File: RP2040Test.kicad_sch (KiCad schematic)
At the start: 1 part

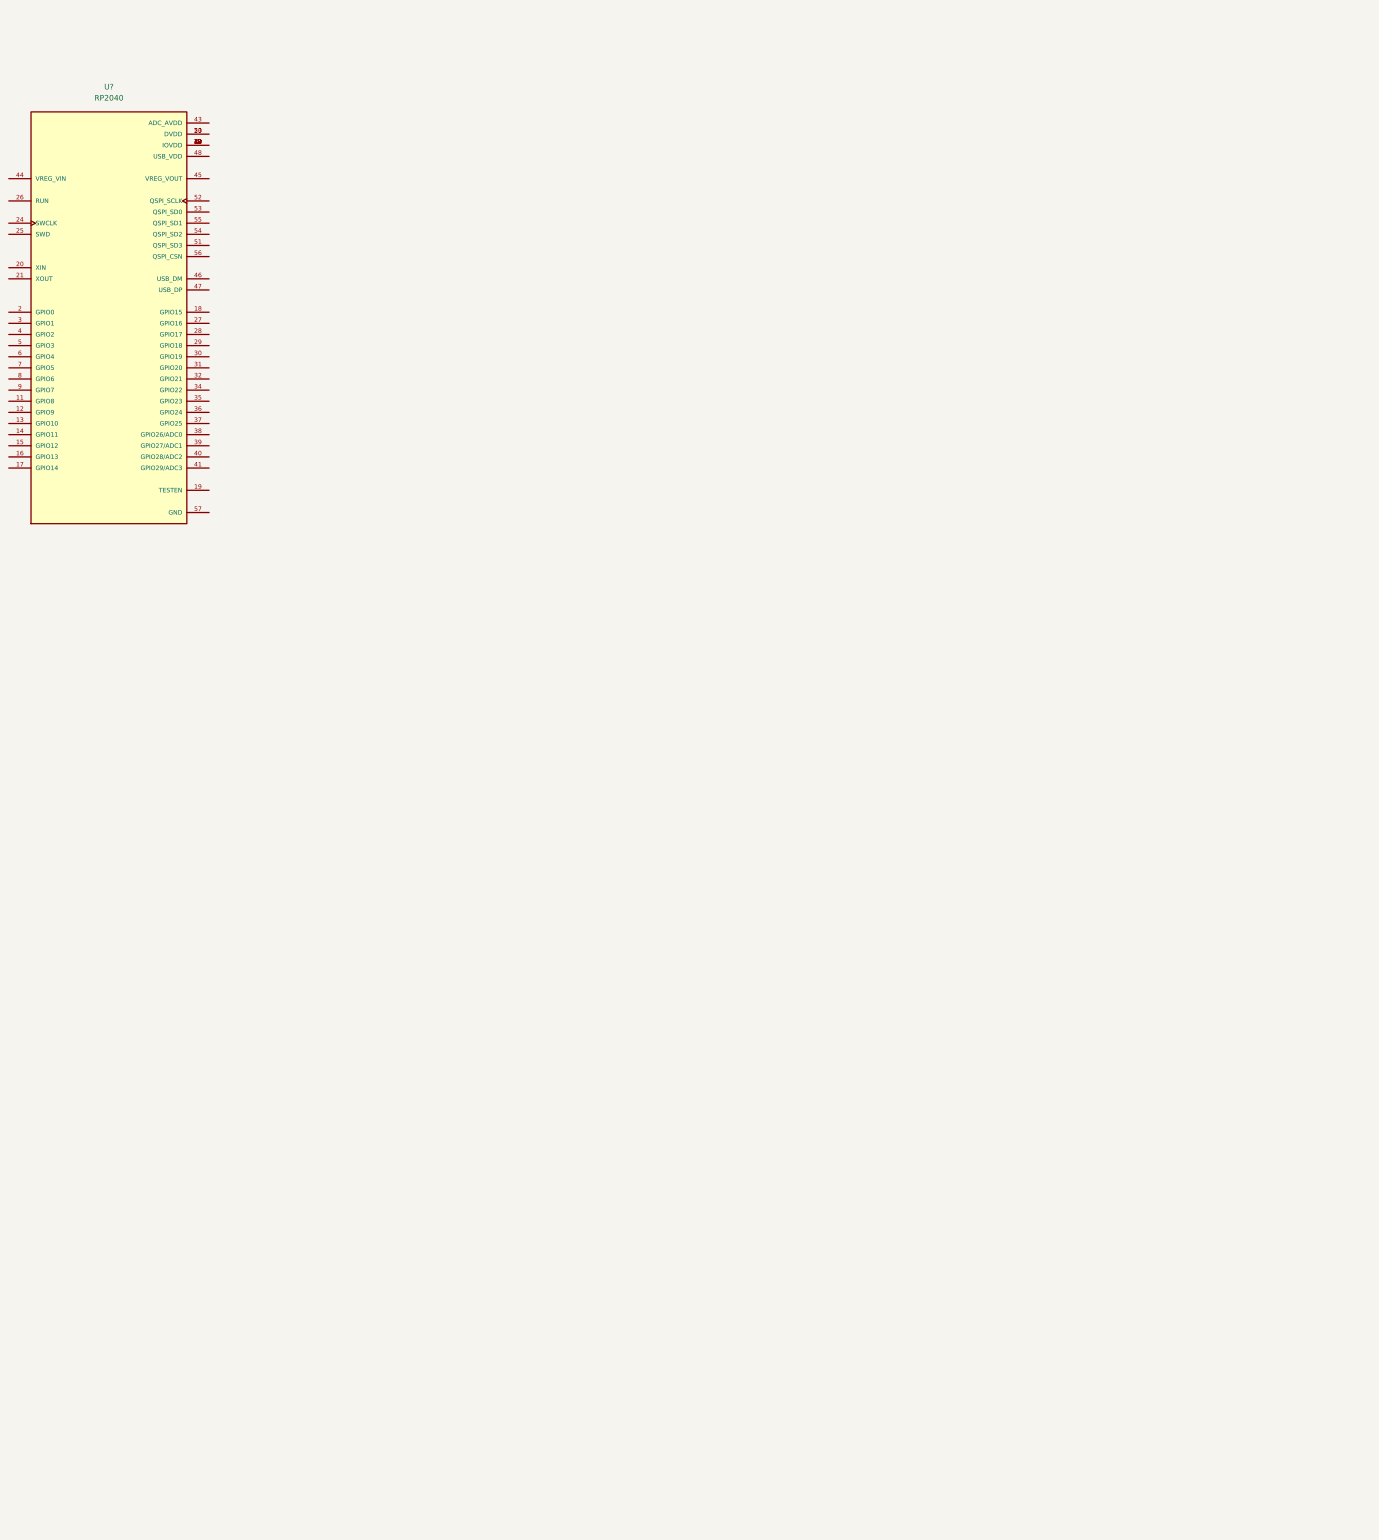
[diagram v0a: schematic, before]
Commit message: laid out electronics for mcu usb and solenoid, double check how power supply will work
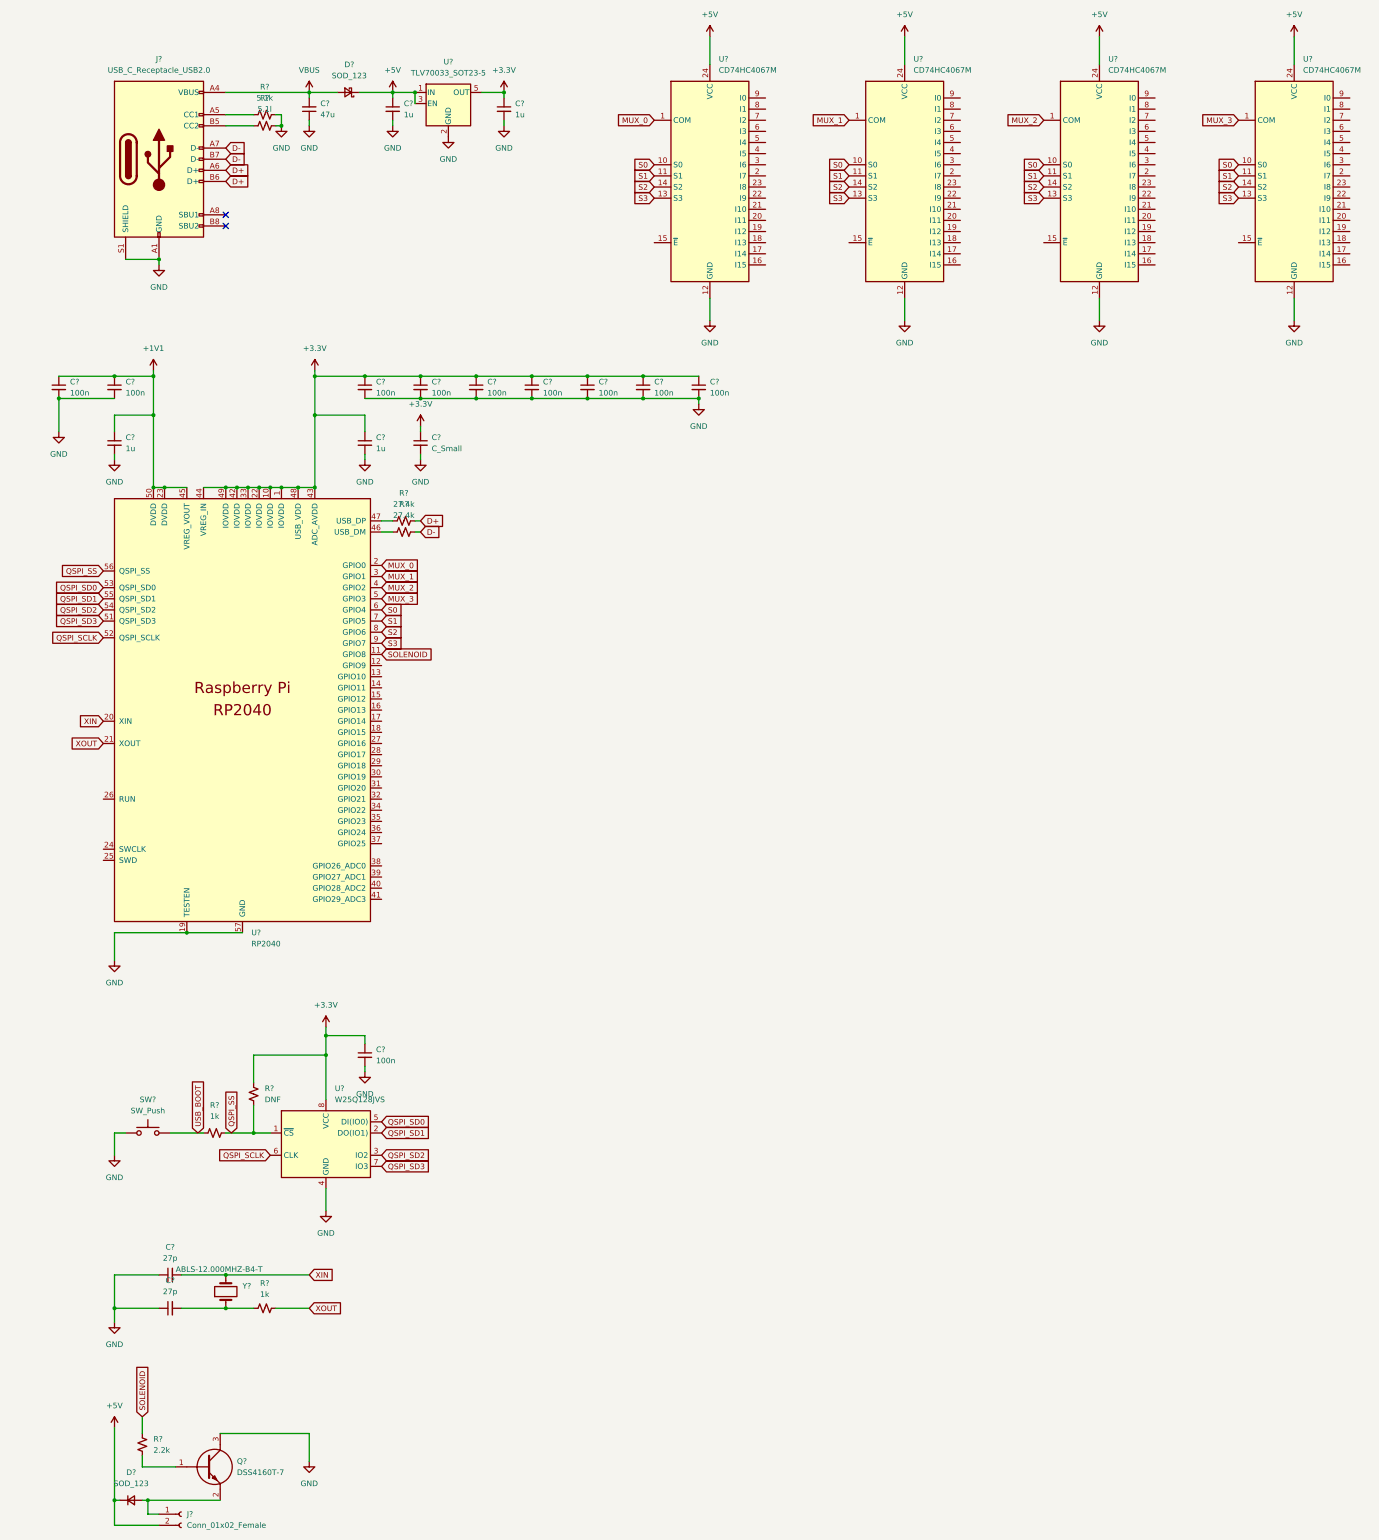
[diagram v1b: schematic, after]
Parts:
- removed U?: RP2040, QFN40P700X700X90-57N, symbol RP2040:RP2040
- added C? (x10): 100n, symbol Device:C_Small
- added C? (x2): 27p, symbol Device:C_Small
- added C?: 47u, symbol Device:C_Small
- added C? (x4): 1u, symbol Device:C_Small
- added C?: C_Small, symbol Device:C_Small
- added D?: SOD_123, symbol Device:D_Schottky_Small
- added D?: SOD_123, symbol Device:D_Small
- added J?: USB_C_Receptacle_USB2.0, symbol Connector:USB_C_Receptacle_USB2.0
- added J?: Conn_01x02_Female, symbol Connector:Conn_01x02_Female
- added Q?: DSS4160T-7, SOT95P240X120-3N, symbol DSS4160T-7:DSS4160T-7
- added R?: 5.1k, symbol Device:R_Small_US
- added R?: 5.1l, symbol Device:R_Small_US
- added R?: DNF, symbol Device:R_Small_US
- added R?: 2.2k, symbol Device:R_Small_US
- added R? (x2): 1k, symbol Device:R_Small_US
- added R? (x2): 27.4k, symbol Device:R_Small_US
- added SW?: SW_Push, symbol Switch:SW_Push
- added U? (x4): CD74HC4067M, Package_SO:SOIC-24W_7.5x15.4mm_P1.27mm, symbol 74xx:CD74HC4067M
- added U?: TLV70033_SOT23-5, Package_TO_SOT_SMD:SOT-23-5, symbol Regulator_Linear:TLV70033_SOT23-5
- added U?: W25Q128JVS, Package_SO:SOIC-8_5.23x5.23mm_P1.27mm, symbol Memory_Flash:W25Q128JVS
- added U?: RP2040, RP2040_minimal:RP2040-QFN-56, symbol MCU_RaspberryPi_RP2040:RP2040
- added Y?: ABLS-12.000MHZ-B4-T, symbol Device:Crystal
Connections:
- new net: J?.A5 (CC1), R?.1
- new net: J?.B5 (CC2), R?.2
- new net: D?.2 (A), J?.1 (Pin_1), Q?.2
- new net: Q?.1, R?.2
- new net: R?.1, U?.46 (USB_DM)
- new net: C?.2, R?.1, Y?.1
- new net: U?.1 (IOVDD), U?.10 (IOVDD), U?.22 (IOVDD), U?.33 (IOVDD), U?.42 (IOVDD), U?.43 (ADC_AVDD), U?.44 (VREG_IN), U?.48 (USB_VDD), U?.49 (IOVDD)
- new net: U?.23 (DVDD), U?.45 (VREG_VOUT), U?.50 (DVDD)
- new net: R?.1, U?.47 (USB_DP)
- new net +1V1: C?.1, C?.1, C?.1
- new net +3.3V: C?.1, C?.1, C?.1, C?.1, C?.1, C?.1, C?.1, C?.1, C?.1, C?.1, C?.1, R?.1, U?.5 (OUT), U?.8 (VCC)
- new net +5V: C?.1, D?.1 (K), D?.1 (K), J?.2 (Pin_2), U?.1 (IN), U?.24 (VCC), U?.24 (VCC), U?.24 (VCC), U?.24 (VCC), U?.3 (EN)
- new net D+: J?.A6 (D+), J?.B6 (D+), R?.2
- new net D-: J?.A7 (D-), J?.B7 (D-), R?.2
- new net GND: C?.1, C?.1, C?.1, C?.2, C?.2, C?.2, C?.2, C?.2, C?.2, C?.2, C?.2, C?.2, C?.2, C?.2, C?.2, C?.2, C?.2, C?.2, J?.A1 (GND), J?.A12 (GND), J?.B1 (GND), J?.B12 (GND), J?.S1 (SHIELD), Q?.3, R?.1, R?.2, SW?.1, U?.12 (GND), U?.12 (GND), U?.12 (GND), U?.19 (TESTEN), U?.2 (GND), U?.4 (GND), U?.57 (GND)
- new net MUX_0: U?.1 (COM), U?.2 (GPIO0)
- new net MUX_1: U?.1 (COM), U?.3 (GPIO1)
- new net MUX_2: U?.1 (COM), U?.4 (GPIO2)
- new net MUX_3: U?.1 (COM), U?.5 (GPIO3)
- new net QSPI_SCLK: U?.52 (QSPI_SCLK), U?.6 (CLK)
- new net QSPI_SD0: U?.5 (DI(IO0)), U?.53 (QSPI_SD0)
- new net QSPI_SD1: U?.2 (DO(IO1)), U?.55 (QSPI_SD1)
- new net QSPI_SD2: U?.3 (IO2), U?.54 (QSPI_SD2)
- new net QSPI_SD3: U?.51 (QSPI_SD3), U?.7 (IO3)
- new net QSPI_SS: R?.2, R?.2, U?.1 (~{CS}), U?.56 (QSPI_SS)
- new net S0: U?.10 (S0), U?.10 (S0), U?.10 (S0), U?.10 (S0), U?.6 (GPIO4)
- new net S1: U?.11 (S1), U?.11 (S1), U?.11 (S1), U?.11 (S1), U?.7 (GPIO5)
- new net S2: U?.14 (S2), U?.14 (S2), U?.14 (S2), U?.14 (S2), U?.8 (GPIO6)
- new net S3: U?.13 (S3), U?.13 (S3), U?.13 (S3), U?.13 (S3), U?.9 (GPIO7)
- new net SOLENOID: R?.1, U?.11 (GPIO8)
- new net USB_BOOT: R?.1, SW?.2
- new net VBUS: C?.2, D?.2 (A), J?.A4 (VBUS), J?.A9 (VBUS), J?.B4 (VBUS), J?.B9 (VBUS)
- new net XIN: C?.2, Y?.2
- new net XOUT: R?.2
- no-connect marks 0 -> 2

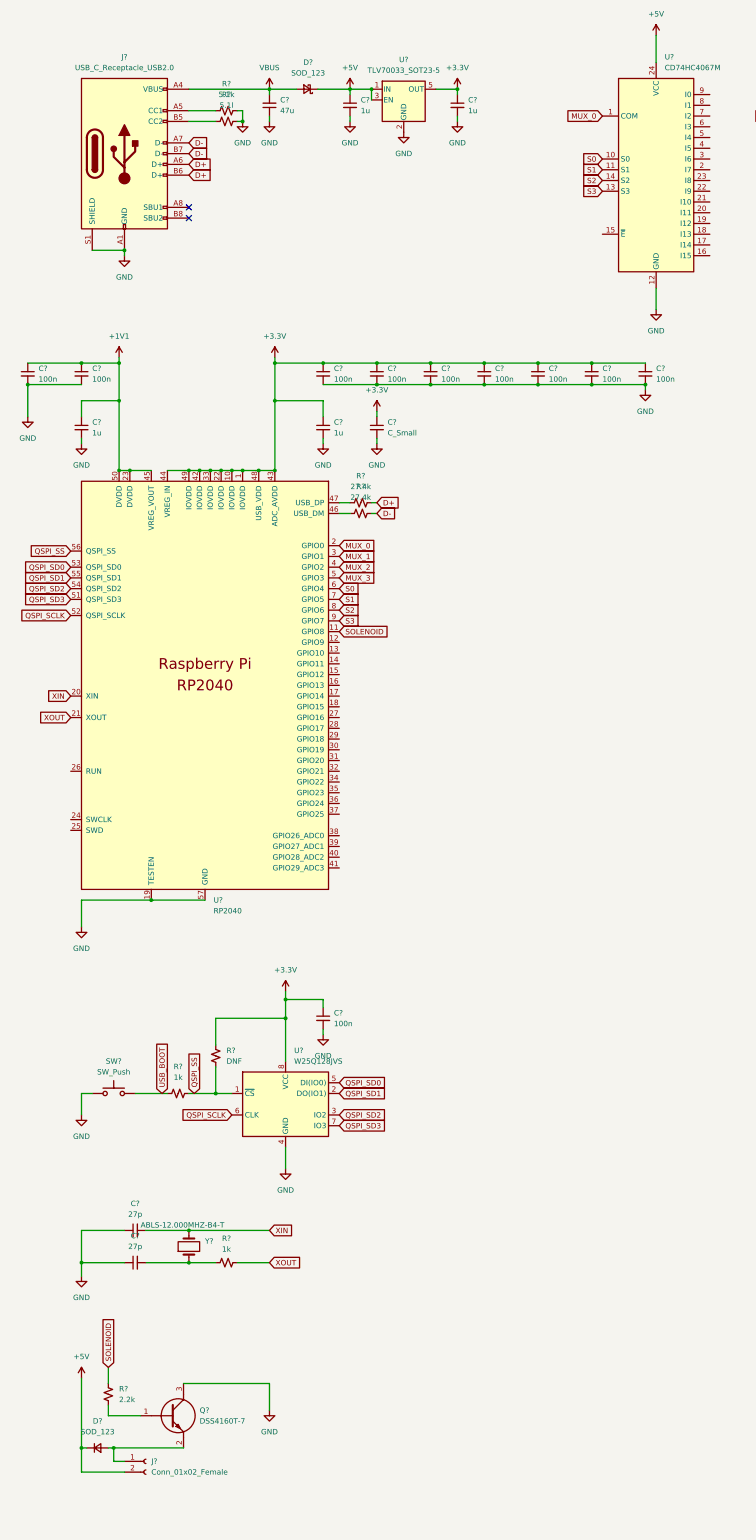
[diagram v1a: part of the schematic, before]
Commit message: changed how 3.3v was converted and how 5v was regulated
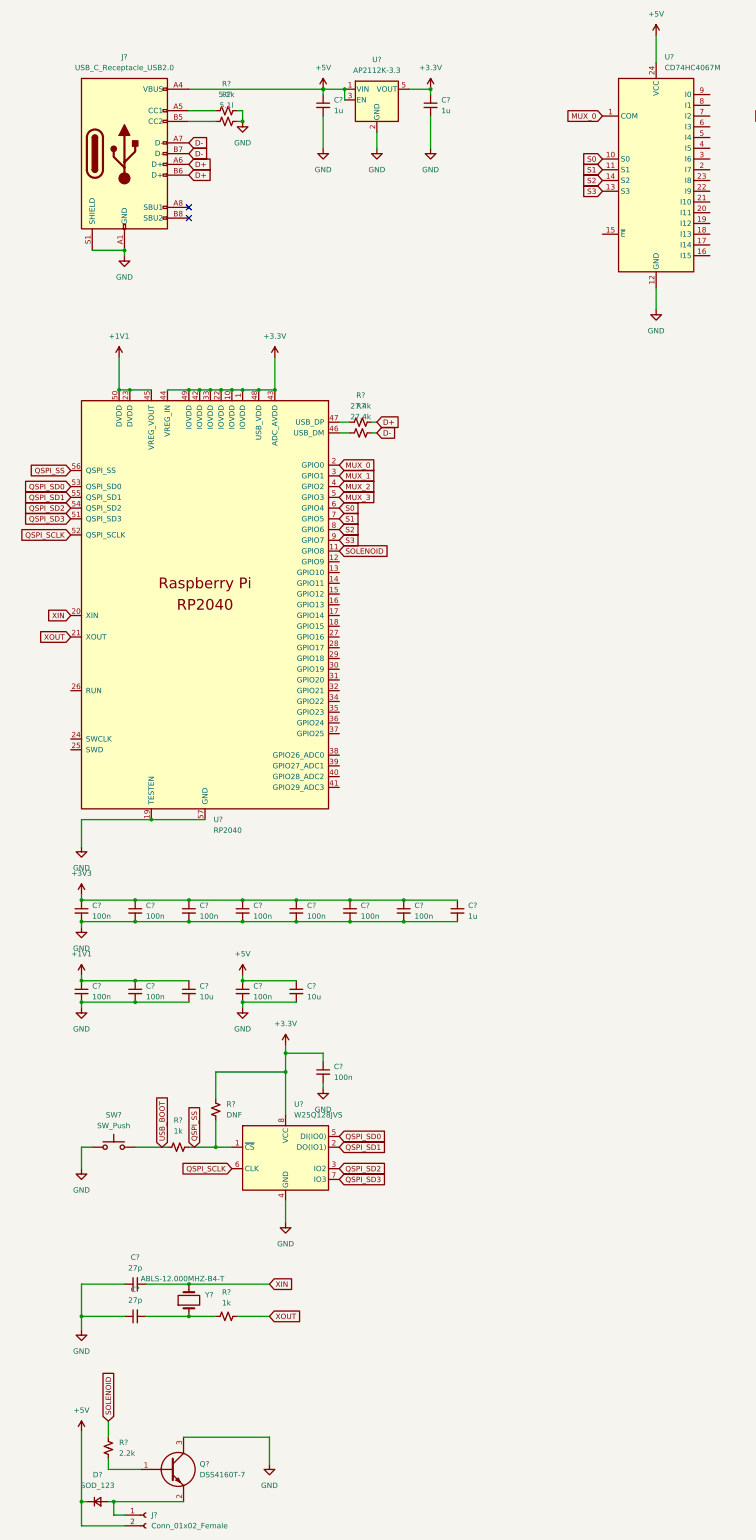
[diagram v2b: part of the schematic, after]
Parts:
- removed C?: 47u, symbol Device:C_Small
- removed C?: C_Small, symbol Device:C_Small
- removed D?: SOD_123, symbol Device:D_Schottky_Small
- removed U?: TLV70033_SOT23-5, Package_TO_SOT_SMD:SOT-23-5, symbol Regulator_Linear:TLV70033_SOT23-5
- added C?: 10u, symbol Device:C_Small
- added C?: 100n, symbol Device:C_Small
- added U?: AP2112K-3.3, Package_TO_SOT_SMD:SOT-23-5, symbol Regulator_Linear:AP2112K-3.3
- C?: value 1u -> 10u
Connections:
- net VBUS is gone; now on net +5V: J?.A4 (VBUS), J?.A9 (VBUS), J?.B4 (VBUS), J?.B9 (VBUS)
- net +1V1: now also U?.23 (DVDD), U?.45 (VREG_VOUT), U?.50 (DVDD)
- net +3.3V: now also U?.1 (IOVDD), U?.10 (IOVDD), U?.22 (IOVDD), U?.33 (IOVDD), U?.42 (IOVDD), U?.43 (ADC_AVDD), U?.44 (VREG_IN), U?.48 (USB_VDD), U?.49 (IOVDD); no longer C?.1, C?.1, C?.1, C?.1, C?.1, C?.1, C?.1, C?.1, C?.1
- net +5V: now also C?.1, C?.1; no longer C?.1
- net GND: now also C?.2, C?.2, U?.2 (GND)
- new net: C?.1, U?.1 (VIN), U?.3 (EN)
- new net: C?.1, U?.5 (VOUT)
- new net +3V3: C?.1, C?.1, C?.1, C?.1, C?.1, C?.1, C?.1, C?.1
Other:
- moved on the sheet: C?, D?, J?, Q?, R?, SW?, U?, Y?

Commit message: added switches and updated type of multiplexer
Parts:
- removed U? (x4): CD74HC4067M, Package_SO:SOIC-24W_7.5x15.4mm_P1.27mm, symbol 74xx:CD74HC4067M
- added MX? (x66): MX-NoLED, symbol MX_Alps_Hybrid:MX-NoLED
- added U? (x17): MAX4634EUB+, SOP50P490X110-10N, symbol MAX4634EUB_:MAX4634EUB+
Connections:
- net +3V3: now also U?.5 (EN), U?.5 (EN), U?.5 (EN), U?.5 (EN), U?.5 (EN), U?.5 (EN), U?.5 (EN), U?.5 (EN), U?.5 (EN), U?.5 (EN), U?.5 (EN), U?.5 (EN), U?.5 (EN), U?.5 (EN), U?.5 (EN), U?.5 (EN), U?.5 (EN), U?.6 (V+), U?.6 (V+), U?.6 (V+), U?.6 (V+), U?.6 (V+), U?.6 (V+), U?.6 (V+), U?.6 (V+), U?.6 (V+), U?.6 (V+), U?.6 (V+), U?.6 (V+), U?.6 (V+), U?.6 (V+), U?.6 (V+), U?.6 (V+), U?.6 (V+)
- net GND: now also MX?.2 (ROW), MX?.2 (ROW), MX?.2 (ROW), MX?.2 (ROW), MX?.2 (ROW), MX?.2 (ROW), MX?.2 (ROW), MX?.2 (ROW), MX?.2 (ROW), MX?.2 (ROW), MX?.2 (ROW), MX?.2 (ROW), MX?.2 (ROW), MX?.2 (ROW), MX?.2 (ROW), MX?.2 (ROW), MX?.2 (ROW), MX?.2 (ROW), MX?.2 (ROW), MX?.2 (ROW), MX?.2 (ROW), MX?.2 (ROW), MX?.2 (ROW), MX?.2 (ROW), MX?.2 (ROW), MX?.2 (ROW), MX?.2 (ROW), MX?.2 (ROW), MX?.2 (ROW), MX?.2 (ROW), MX?.2 (ROW), MX?.2 (ROW), MX?.2 (ROW), MX?.2 (ROW), MX?.2 (ROW), MX?.2 (ROW), MX?.2 (ROW), MX?.2 (ROW), MX?.2 (ROW), MX?.2 (ROW), MX?.2 (ROW), MX?.2 (ROW), MX?.2 (ROW), MX?.2 (ROW), MX?.2 (ROW), MX?.2 (ROW), MX?.2 (ROW), MX?.2 (ROW), MX?.2 (ROW), MX?.2 (ROW), MX?.2 (ROW), MX?.2 (ROW), MX?.2 (ROW), MX?.2 (ROW), MX?.2 (ROW), MX?.2 (ROW), MX?.2 (ROW), MX?.2 (ROW), MX?.2 (ROW), MX?.2 (ROW), MX?.2 (ROW), MX?.2 (ROW), MX?.2 (ROW), MX?.2 (ROW), MX?.2 (ROW), MX?.2 (ROW), U?.3 (GND), U?.3 (GND), U?.3 (GND), U?.3 (GND), U?.3 (GND), U?.3 (GND), U?.3 (GND), U?.3 (GND), U?.3 (GND), U?.3 (GND), U?.3 (GND), U?.3 (GND), U?.3 (GND), U?.3 (GND), U?.3 (GND), U?.3 (GND), U?.3 (GND)
- net SOLENOID: no longer U?.11 (GPIO8)
- net MUX_09: now reaches U?.12 (GPIO9)
- net MUX_09: now also U?.8 (COM)
- net MUX_10: now reaches U?.13 (GPIO10)
- net MUX_10: now also U?.8 (COM)
- net MUX_11: now reaches U?.14 (GPIO11)
- net MUX_11: now also U?.8 (COM)
- net MUX_12: now reaches U?.15 (GPIO12)
- net MUX_12: now also U?.8 (COM)
- net MUX_13: now reaches U?.16 (GPIO13)
- net MUX_13: now also U?.8 (COM)
- net MUX_14: now reaches U?.17 (GPIO14)
- net MUX_14: now also U?.8 (COM)
- net MUX_15: now reaches U?.18 (GPIO15)
- net MUX_15: now also U?.8 (COM)
- net MUX_16: now reaches U?.27 (GPIO16)
- net MUX_16: now also U?.8 (COM)
- net A0: now reaches U?.28 (GPIO17)
- net A0: now also U?.1 (A0), U?.1 (A0), U?.1 (A0), U?.1 (A0), U?.1 (A0), U?.1 (A0), U?.1 (A0), U?.1 (A0), U?.1 (A0), U?.1 (A0), U?.1 (A0), U?.1 (A0), U?.1 (A0), U?.1 (A0), U?.1 (A0), U?.1 (A0), U?.1 (A0)
- net A1: now reaches U?.29 (GPIO18)
- net A1: now also U?.10 (A1), U?.10 (A1), U?.10 (A1), U?.10 (A1), U?.10 (A1), U?.10 (A1), U?.10 (A1), U?.10 (A1), U?.10 (A1), U?.10 (A1), U?.10 (A1), U?.10 (A1), U?.10 (A1), U?.10 (A1), U?.10 (A1), U?.10 (A1), U?.10 (A1)
- net MUX_0 renamed MUX_00
- net MUX_00: now also U?.8 (COM)
- net MUX_1 renamed MUX_01
- net MUX_01: now also U?.8 (COM)
- net MUX_2 renamed MUX_02
- net MUX_02: now also U?.8 (COM)
- net MUX_3 renamed MUX_03
- net MUX_03: now also U?.8 (COM)
- net S0 renamed MUX_04
- net MUX_04: now also U?.8 (COM)
- net S1 renamed MUX_05
- net MUX_05: now also U?.8 (COM)
- net S2 renamed MUX_06
- net MUX_06: now also U?.8 (COM)
- net S3 renamed MUX_07
- net MUX_07: now also U?.8 (COM)
- new net MUX_08: U?.11 (GPIO8), U?.8 (COM)
- new net SW_00: MX?.1 (COL), U?.2 (N01)
- new net SW_01: MX?.1 (COL), U?.9 (N02)
- new net SW_02: MX?.1 (COL), U?.4 (N03)
- new net SW_03: MX?.1 (COL), U?.7 (NO4)
- new net SW_04: MX?.1 (COL), U?.2 (N01)
- new net SW_05: MX?.1 (COL), U?.9 (N02)
- new net SW_06: MX?.1 (COL), U?.4 (N03)
- new net SW_07: MX?.1 (COL), U?.7 (NO4)
- new net SW_08: MX?.1 (COL), U?.2 (N01)
- new net SW_09: MX?.1 (COL), U?.9 (N02)
- new net SW_10: MX?.1 (COL), U?.4 (N03)
- new net SW_11: MX?.1 (COL), U?.7 (NO4)
- new net SW_12: MX?.1 (COL), U?.2 (N01)
- new net SW_13: MX?.1 (COL), U?.9 (N02)
- new net SW_14: MX?.1 (COL), U?.4 (N03)
- new net SW_15: MX?.1 (COL), U?.7 (NO4)
- new net SW_16: MX?.1 (COL), U?.2 (N01)
- new net SW_17: MX?.1 (COL), U?.9 (N02)
- new net SW_18: MX?.1 (COL), U?.4 (N03)
- new net SW_19: MX?.1 (COL), U?.7 (NO4)
- new net SW_20: MX?.1 (COL), U?.2 (N01)
- new net SW_21: MX?.1 (COL), U?.9 (N02)
- new net SW_22: MX?.1 (COL), U?.4 (N03)
- new net SW_23: MX?.1 (COL), U?.7 (NO4)
- new net SW_24: MX?.1 (COL), U?.2 (N01)
- new net SW_25: MX?.1 (COL), U?.9 (N02)
- new net SW_26: MX?.1 (COL), U?.4 (N03)
- new net SW_27: MX?.1 (COL), U?.7 (NO4)
- new net SW_28: MX?.1 (COL), U?.2 (N01)
- new net SW_29: MX?.1 (COL), U?.9 (N02)
- new net SW_30: MX?.1 (COL), U?.4 (N03)
- new net SW_31: MX?.1 (COL), U?.7 (NO4)
- new net SW_32: MX?.1 (COL), U?.2 (N01)
- new net SW_33: MX?.1 (COL), U?.9 (N02)
- new net SW_34: MX?.1 (COL), U?.4 (N03)
- new net SW_35: MX?.1 (COL), U?.7 (NO4)
- new net SW_36: MX?.1 (COL), U?.2 (N01)
- new net SW_37: MX?.1 (COL), U?.9 (N02)
- new net SW_38: MX?.1 (COL), U?.4 (N03)
- new net SW_39: MX?.1 (COL), U?.7 (NO4)
- new net SW_40: MX?.1 (COL), U?.2 (N01)
- new net SW_41: MX?.1 (COL), U?.9 (N02)
- new net SW_42: MX?.1 (COL), U?.4 (N03)
- new net SW_43: MX?.1 (COL), U?.7 (NO4)
- new net SW_44: MX?.1 (COL), U?.2 (N01)
- new net SW_45: MX?.1 (COL), U?.9 (N02)
- new net SW_46: MX?.1 (COL), U?.4 (N03)
- new net SW_47: MX?.1 (COL), U?.7 (NO4)
- new net SW_48: MX?.1 (COL), U?.2 (N01)
- new net SW_49: MX?.1 (COL), U?.9 (N02)
- new net SW_50: MX?.1 (COL), U?.4 (N03)
- new net SW_51: MX?.1 (COL), U?.7 (NO4)
- new net SW_52: MX?.1 (COL), U?.2 (N01)
- new net SW_53: MX?.1 (COL), U?.9 (N02)
- new net SW_54: MX?.1 (COL), U?.4 (N03)
- new net SW_55: MX?.1 (COL), U?.7 (NO4)
- new net SW_56: MX?.1 (COL), U?.2 (N01)
- new net SW_57: MX?.1 (COL), U?.9 (N02)
- new net SW_58: MX?.1 (COL), U?.4 (N03)
- new net SW_59: MX?.1 (COL), U?.7 (NO4)
- new net SW_60: MX?.1 (COL), U?.2 (N01)
- new net SW_61: MX?.1 (COL), U?.9 (N02)
- new net SW_62: MX?.1 (COL), U?.4 (N03)
- new net SW_63: MX?.1 (COL), U?.7 (NO4)
- new net SW_64: MX?.1 (COL), U?.2 (N01)
- new net SW_65: MX?.1 (COL), U?.9 (N02)
